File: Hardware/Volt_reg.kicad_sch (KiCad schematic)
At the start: 26 parts, among them Q2 BSZ025N04LS, Q3 BSZ025N04LS, U10 TPS55288QRPMRQ1

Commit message: V2 changes, PCB finished
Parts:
- removed R51: 110k, Resistor_SMD:R_0402_1005Metric, symbol Device:R_Small
- R53: value 110k -> 56k
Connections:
- net PyroPWR: no longer C46.1, C47.2, R49.1, U10.11 (VOUT_1), U10.12 (ISP), U10.26 (VOUT_2)
- net SW2_2: now also C52.2; no longer C52.1
- net at U10.20 (BOOT2): now also C52.1; no longer C52.2
- new net ISP: C46.1, C47.2, R49.1, U10.11 (VOUT_1), U10.12 (ISP), U10.26 (VOUT_2)
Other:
- moved on the sheet: C52
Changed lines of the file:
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@@
-	)
-	(junction
-		(at 123.19 157.48)
-		(diameter 0)
-		(color 0 0 0 0)
 	)
 	(junction
@@
 	)
 	(junction
-		(at 133.35 156.21)
-		(diameter 0)
-		(color 0 0 0 0)
-	)
-	(junction
 		(at 35.56 162.56)
 		(diameter 0)
@@
 	(wire
 		(pts
-			(xy 129.54 153.67) (xy 133.35 153.67)
-		)
-		(stroke
-			(width 0)
-			(type default)
-		)
-	)
-	(wire
-		(pts
 			(xy 57.15 160.02) (xy 72.39 160.02)
 		)
@@
 	(wire
 		(pts
-			(xy 133.35 153.67) (xy 133.35 156.21)
-		)
-		(stroke
-			(width 0)
-			(type default)
-		)
-	)
-	(wire
-		(pts
 			(xy 46.99 190.5) (xy 53.34 190.5)
 		)
@@
 	(wire
 		(pts
-			(xy 134.62 156.21) (xy 133.35 156.21)
-		)
-		(stroke
-			(width 0)
-			(type default)
-		)
-	)
-	(wire
-		(pts
-			(xy 123.19 157.48) (xy 118.11 157.48)
+			(xy 118.11 157.48) (xy 124.46 157.48)
 		)
 		(stroke
@@
 	(wire
 		(pts
-			(xy 133.35 156.21) (xy 133.35 157.48)
-		)
-		(stroke
-			(width 0)
-			(type default)
-		)
-	)
-	(wire
-		(pts
 			(xy 167.64 156.21) (xy 167.64 158.75)
 		)
@@
 	(wire
 		(pts
-			(xy 156.21 55.88) (xy 165.1 55.88)
-		)
-		(stroke
-			(width 0)
-			(type default)
-		)
-	)
-	(wire
-		(pts
 			(xy 39.37 185.42) (xy 39.37 181.61)
 		)
@@
 	(wire
 		(pts
-			(xy 123.19 153.67) (xy 123.19 157.48)
-		)
-		(stroke
-			(width 0)
-			(type default)
-		)
-	)
-	(wire
-		(pts
-			(xy 124.46 157.48) (xy 123.19 157.48)
-		)
-		(stroke
-			(width 0)
-			(type default)
-		)
-	)
-	(wire
-		(pts
 			(xy 129.54 157.48) (xy 133.35 157.48)
 		)
@@
 		(pts
 			(xy 31.75 162.56) (xy 35.56 162.56)
-		)
-		(stroke
-			(width 0)
-			(type default)
-		)
-	)
-	(wire
-		(pts
-			(xy 123.19 153.67) (xy 124.46 153.67)
 		)
 		(stroke
@@
 		)
 	)
+	(label "ISN"
+		(at 40.64 181.61 180)
+		(effects
+			(font
+				(size 1.27 1.27)
+			)
+			(justify right bottom)
+		)
+	)
 	(label "AGND"
 		(at 33.02 172.72 0)
@@
 	)
 	(label "VOUT"
-		(at 156.21 55.88 180)
-		(effects
-			(font
-				(size 1.27 1.27)
-			)
-			(justify right bottom)
-		)
-	)
-	(label "VOUT"
 		(at 118.11 180.34 0)
+		(effects
+			(font
+				(size 1.27 1.27)
+			)
+			(justify left bottom)
+		)
+	)
+	(label "ISP"
+		(at 45.72 181.61 0)
 		(effects
 			(font
@@
 	)
 	(label "AGND"
-		(at 134.62 156.21 0)
+		(at 133.35 157.48 0)
 		(effects
 			(font
@@
 			)
 			(justify right)
-		)
-	)
-	(hierarchical_label "PyroPWR"
-		(shape output)
-		(at 165.1 55.88 0)
-		(effects
-			(font
-				(size 1.27 1.27)
-			)
-			(justify left)
 		)
 	)
@@
 			)
 		)
-		(property "Value" "110k"
+		(property "Value" "56k"
 			(at 128.016 155.702 90)
 			(effects
@@
 	(symbol
 		(lib_id "Device:C")
-		(at 125.73 165.1 270)
+		(at 125.73 165.1 90)
+		(mirror x)
 		(unit 1)
 		(exclude_from_sim no)
@@
 		(dnp no)
 		(property "Reference" "C52"
-			(at 126.746 164.084 90)
+			(at 124.714 164.084 90)
 			(effects
 				(font
@@
 		)
 		(property "Value" "0.1uF"
-			(at 119.38 164.084 90)
+			(at 132.08 164.084 90)
 			(effects
 				(font
@@
 		)
 		(property "Footprint" "Capacitor_SMD:C_0402_1005Metric"
-			(at 121.92 166.0652 0)
+			(at 129.54 166.0652 0)
 			(effects
 				(font
@@
 					(unit 1)
 				)
-			)
-		)
-	)
-	(symbol
-		(lib_id "Device:R_Small")
-		(at 127 153.67 270)
-		(unit 1)
-		(exclude_from_sim no)
-		(in_bom yes)
-		(on_board yes)
-		(dnp no)
-		(property "Reference" "R51"
-			(at 122.428 151.892 90)
-			(effects
-				(font
-					(size 1.27 1.27)
-				)
-				(justify left)
-			)
-		)
-		(property "Value" "110k"
-			(at 126.746 151.892 90)
-			(effects
-				(font
-					(size 1.27 1.27)
-				)
-				(justify left)
-			)
-		)
-		(property "Footprint" "Resistor_SMD:R_0402_1005Metric"
-			(at 127 153.67 0)
-			(effects
-				(font
-					(size 1.27 1.27)
-				)
-				(hide yes)
-			)
-		)
-		(property "Datasheet" "~"
-			(at 127 153.67 0)
-			(effects
-				(font
-					(size 1.27 1.27)
-				)
-				(hide yes)
-			)
-		)
-		(property "Description" "Resistor, small symbol"
-			(at 127 153.67 0)
-			(effects
-				(font
-					(size 1.27 1.27)
-				)
-				(hide yes)
-			)
-		)
-		(pin "1"
-		)
-		(pin "2"
-		)
-		(instances
-			(project "Main board"
-				(path "/7db990e4-92e1-4f99-b4d2-435bbec1ba83/ab7b921d-66d3-49d7-abff-63184671bf46"
-					(reference "R51")
-					(unit 1)
-				)

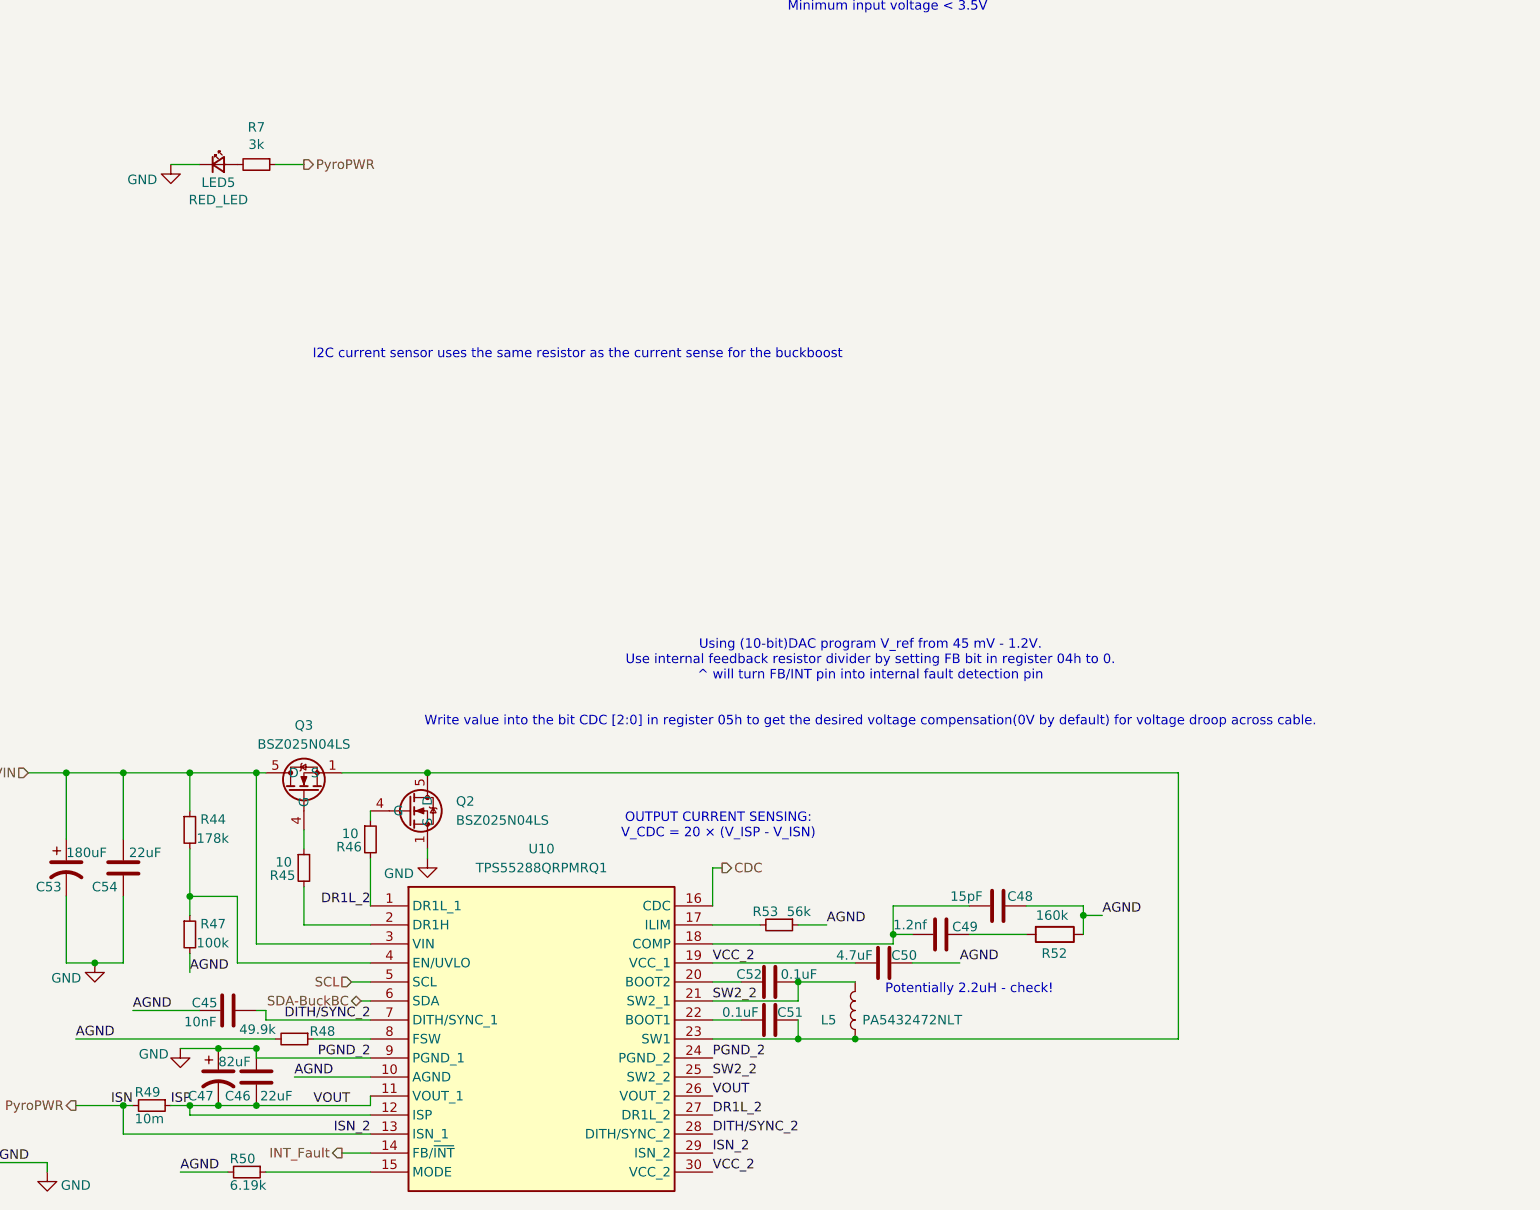
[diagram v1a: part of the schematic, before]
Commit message: More V2 changes
Mainly changed to use Ω symbol for resistors. Fixed the CDC pin for the buck boost
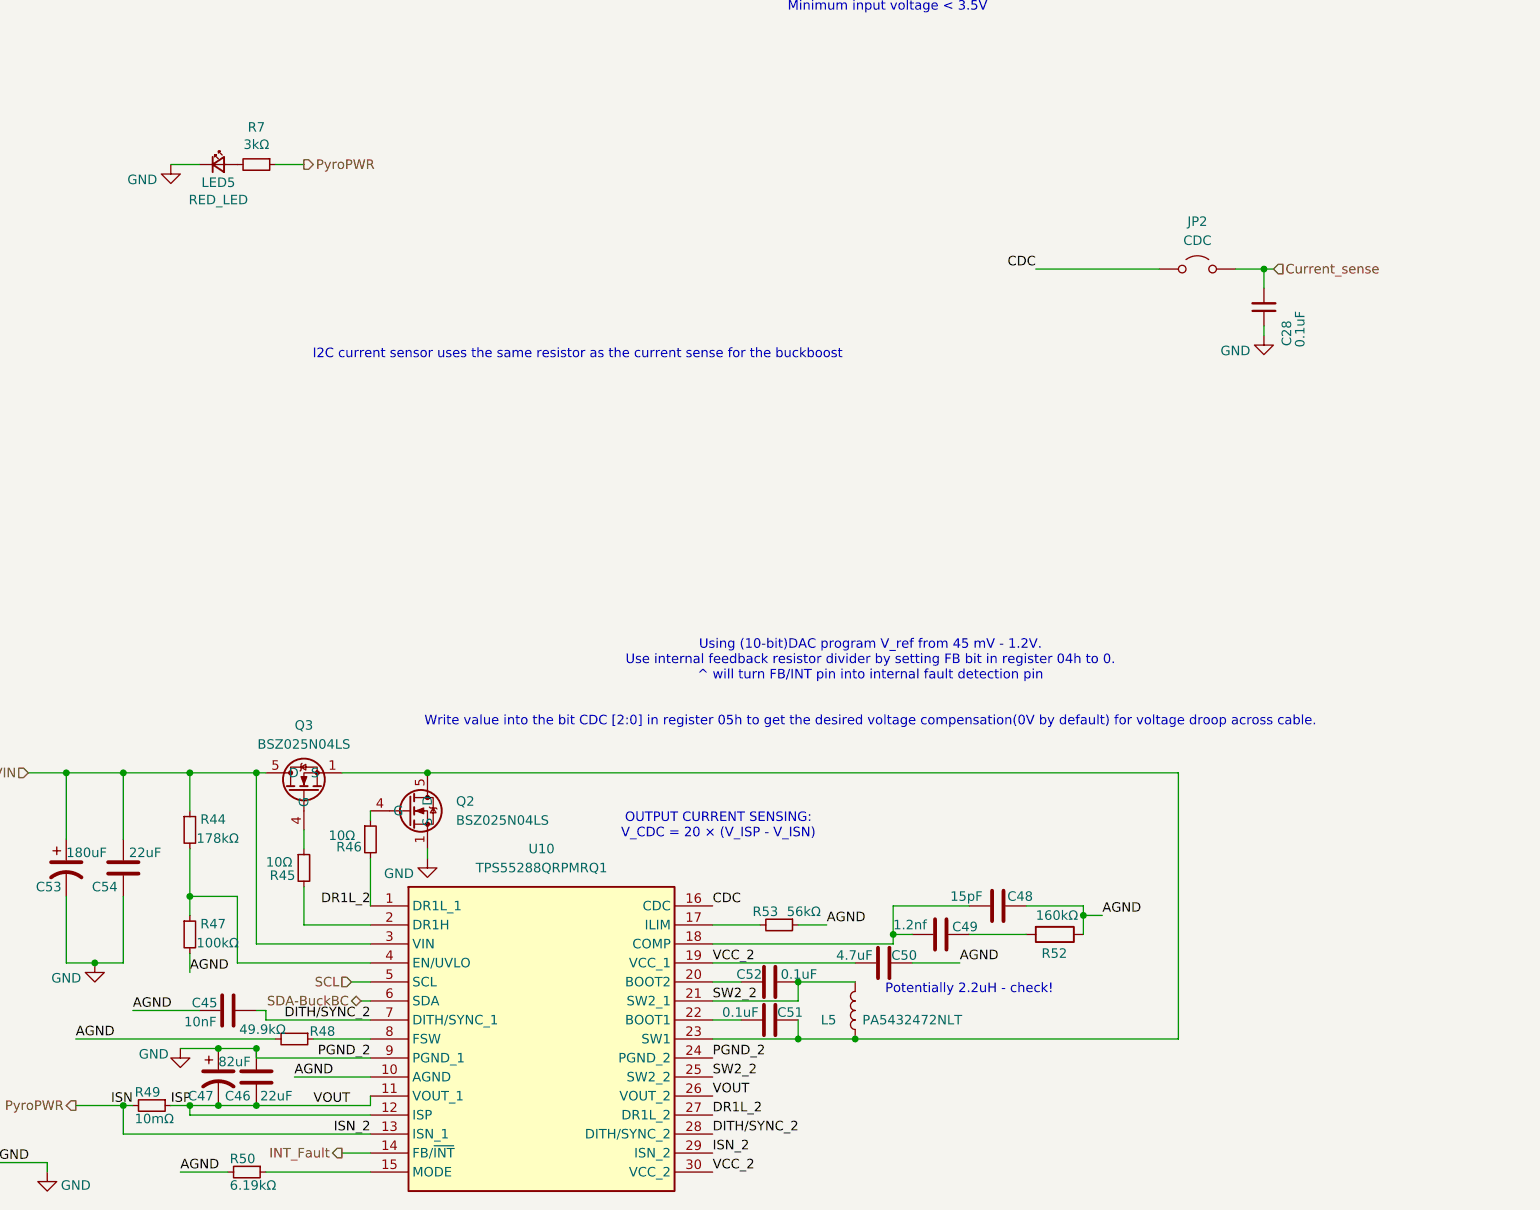
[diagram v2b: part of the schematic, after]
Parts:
- added C28: 0.1uF, Capacitor_SMD:C_0402_1005Metric, symbol Device:C_Small
- added JP2: CDC, Capacitor_SMD:C_0402_1005Metric_Pad0.74x0.62mm_HandSolder, symbol Jumper:Jumper_2_Open
- R44: value 178k -> 178kΩ
- R45, R46: value 10 -> 10Ω
- R47: value 100k -> 100kΩ
- R48: value 49.9k -> 49.9kΩ
- R49: value 10m -> 10mΩ
- R50: value 6.19k -> 6.19kΩ
- R52: value 160k -> 160kΩ
- R53: value 56k -> 56kΩ
- R7: value 3k -> 3kΩ
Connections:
- net CDC: now also JP2.1 (A)
- net GND: now also C28.1
- new net Current_sense: C28.2, JP2.2 (B)

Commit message: reformatted and renamed file
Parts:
- C306: renamed from C52; value 0.1uF -> 100nF
- C307: renamed from C51; value 0.1uF -> 100nF
- C309: renamed from C49; value 1.2nf -> 1.2nF
- C311: renamed from C28; value 0.1uF -> 100nF
- JP301: renamed from JP2; now left out of the parts list
- L301: renamed from L5; value PA5432472NLT -> 4.7uH; MPN (none) -> PA5432472NLT
- LED301: renamed from LED5; value RED_LED -> LED_RED
- renumbered C53 to C301, C54 to C302, C47 to C303, C45 to C304, C46 to C305, C50 to C308, C48 to C310, Q3 to Q301, Q2 to Q302, R49 to R301, R44 to R302, R47 to R303, R50 to R304, R7 to R305, R48 to R306, R45 to R307, R46 to R308, R53 to R309, R52 to R310, U10 to U301
